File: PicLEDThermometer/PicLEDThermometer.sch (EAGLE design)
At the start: 13 parts, among them IC1 74LS595N, X1 1751248

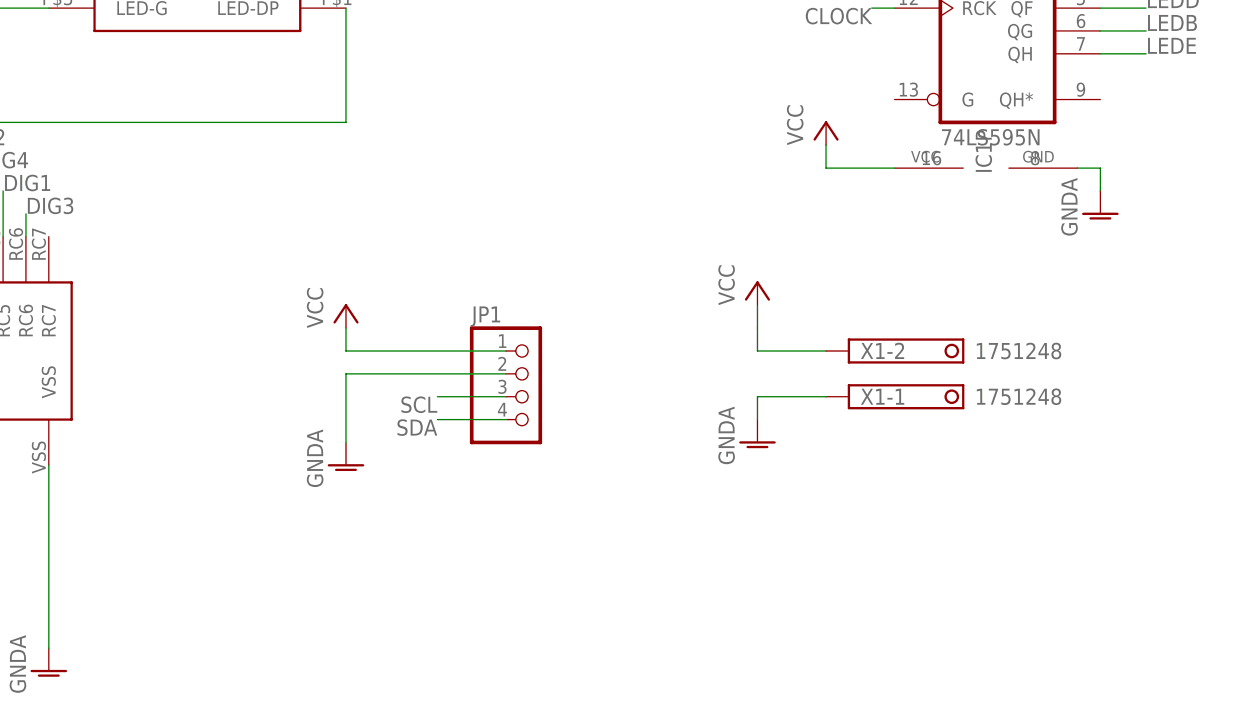
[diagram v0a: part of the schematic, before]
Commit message: Add a voltage regulator.
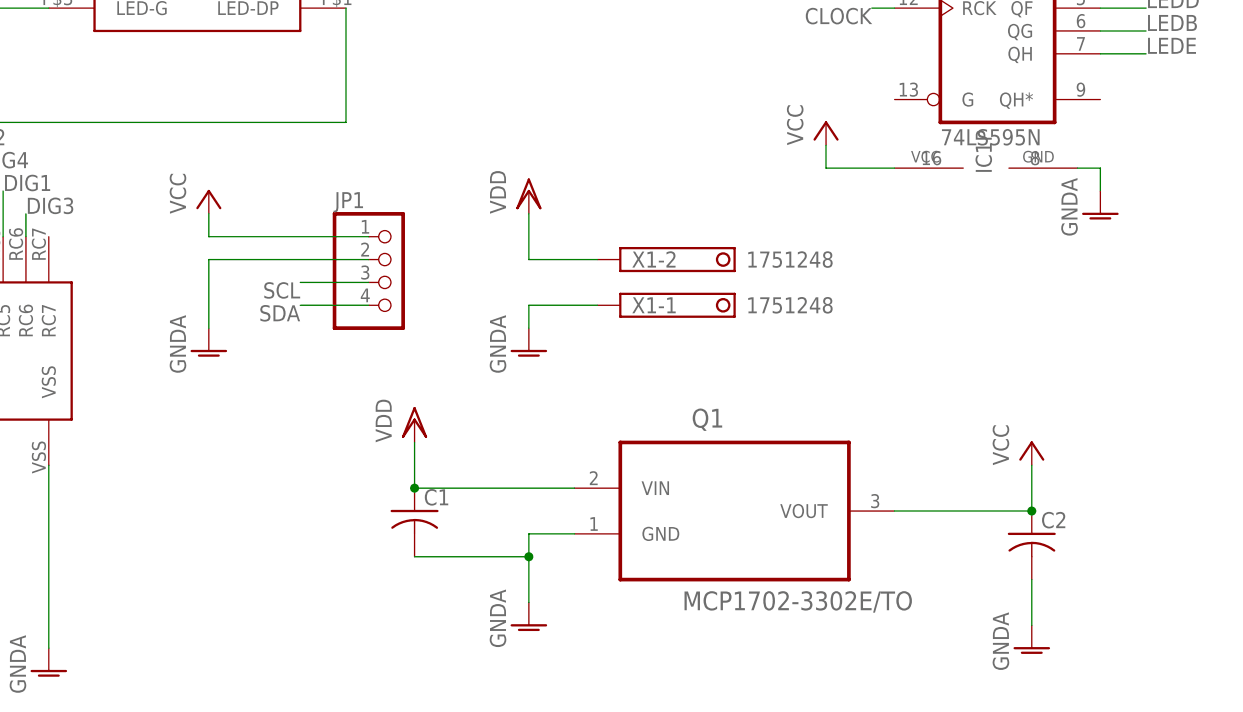
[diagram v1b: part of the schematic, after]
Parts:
- added C1, C2: (no value), rcl:C-US025-030X050
- added Q1: MCP1702-3302E/TO, Microchip_By_element14_Batch_1:MCP1702-3302E/TO
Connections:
- new net VDD: C1.1, Q1.VIN, X1-2.K
- net GNDA: now also C1.2, C2.2, Q1.GND
- net VCC: now also C2.1, Q1.VOUT; no longer X1-2.K
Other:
- moved on the sheet: JP1, X1-1, X1-2

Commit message: Change power input to padded holes.
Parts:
- removed X1: 1751248, con-phoenix-350:1751248
- added H1, H2: MOUNT-PAD-ROUND2.8, holes:MOUNT-PAD-ROUND2.8
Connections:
- net GNDA: now also H2.MOUNT; no longer X1-1.K
- net VDD: now also H1.MOUNT; no longer X1-2.K
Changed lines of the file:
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@@
 <?xml version="1.0" encoding="utf-8"?>
 <!DOCTYPE eagle SYSTEM "eagle.dtd">
-<eagle version="9.1.3">
+<eagle version="8.2.2">
 <drawing>
 <settings>
 <setting alwaysvectorfont="no"/>
-<setting keepoldvectorfont="yes"/>
 <setting verticaltext="up"/>
 </settings>
@@
 <part name="GND3" library="supply1" library_urn="urn:adsk.eagle:library:371" deviceset="GNDA" device=""/>
 <part name="P+3" library="supply1" library_urn="urn:adsk.eagle:library:371" deviceset="VCC" device=""/>
-<part name="X1" library="con-phoenix-350" library_urn="urn:adsk.eagle:library:174" deviceset="1751248" device=""/>
-<part name="GND4" library="supply1" library_urn="urn:adsk.eagle:library:371" deviceset="GNDA" device=""/>
 <part name="Q1" library="Microchip_By_element14_Batch_1" deviceset="MCP1702-3302E/TO" device=""/>
 <part name="GND5" library="supply1" library_urn="urn:adsk.eagle:library:371" deviceset="GNDA" device=""/>
 <part name="P+5" library="supply1" library_urn="urn:adsk.eagle:library:371" deviceset="VCC" device=""/>
 <part name="VDD1" library="supply1" deviceset="VDD" device=""/>
-<part name="VDD2" library="supply1" deviceset="VDD" device=""/>
-<part name="C1" library="rcl" library_urn="urn:adsk.eagle:library:334" deviceset="C-US" device="025-030X050" package3d_urn="urn:adsk.eagle:package:23631/1"/>
-<part name="C2" library="rcl" library_urn="urn:adsk.eagle:library:334" deviceset="C-US" device="025-030X050" package3d_urn="urn:adsk.eagle:package:23631/1"/>
+<part name="C1" library="rcl" library_urn="urn:adsk.eagle:library:334" deviceset="C-US" device="025-030X050"/>
+<part name="C2" library="rcl" library_urn="urn:adsk.eagle:library:334" deviceset="C-US" device="025-030X050"/>
 <part name="GND6" library="supply1" library_urn="urn:adsk.eagle:library:371" deviceset="GNDA" device=""/>
+<part name="H1" library="holes" library_urn="urn:adsk.eagle:library:237" deviceset="MOUNT-PAD-ROUND" device="2.8" value="MOUNT-PAD-ROUND2.8"/>
+<part name="H2" library="holes" library_urn="urn:adsk.eagle:library:237" deviceset="MOUNT-PAD-ROUND" device="2.8" value="MOUNT-PAD-ROUND2.8"/>
+<part name="VDD3" library="supply1" deviceset="VDD" device=""/>
+<part name="GND7" library="supply1" library_urn="urn:adsk.eagle:library:371" deviceset="GNDA" device=""/>
 </parts>
 <sheets>
@@
 <instance part="GND3" gate="1" x="170.18" y="40.64"/>
 <instance part="P+3" gate="VCC" x="139.7" y="50.8"/>
-<instance part="X1" gate="-1" x="116.84" y="30.48"/>
-<instance part="X1" gate="-2" x="116.84" y="35.56"/>
-<instance part="GND4" gate="1" x="106.68" y="25.4"/>
 <instance part="Q1" gate="A" x="129.54" y="10.16"/>
 <instance part="GND5" gate="1" x="106.68" y="-5.08"/>
 <instance part="P+5" gate="VCC" x="162.56" y="15.24"/>
 <instance part="VDD1" gate="G$1" x="93.98" y="17.78"/>
-<instance part="VDD2" gate="G$1" x="106.68" y="43.18"/>
 <instance part="C1" gate="G$1" x="93.98" y="7.62"/>
 <instance part="C2" gate="G$1" x="162.56" y="5.08"/>
 <instance part="GND6" gate="1" x="162.56" y="-7.62"/>
+<instance part="H1" gate="G$1" x="124.46" y="38.1"/>
+<instance part="H2" gate="G$1" x="124.46" y="30.48"/>
+<instance part="VDD3" gate="G$1" x="114.3" y="43.18"/>
+<instance part="GND7" gate="1" x="114.3" y="25.4"/>
 </instances>
 <busses>
@@
 <pinref part="GND3" gate="1" pin="GNDA"/>
 <wire x1="170.18" y1="45.72" x2="170.18" y2="43.18" width="0.1524" layer="91"/>
-</segment>
-<segment>
-<pinref part="GND4" gate="1" pin="GNDA"/>
-<wire x1="106.68" y1="30.48" x2="106.68" y2="27.94" width="0.1524" layer="91"/>
-<pinref part="X1" gate="-1" pin="K"/>
-<wire x1="114.3" y1="30.48" x2="106.68" y2="30.48" width="0.1524" layer="91"/>
 </segment>
 <segment>
@@
 <wire x1="162.56" y1="0" x2="162.56" y2="-5.08" width="0.1524" layer="91"/>
 </segment>
+<segment>
+<pinref part="GND7" gate="1" pin="GNDA"/>
+<wire x1="114.3" y1="30.48" x2="114.3" y2="27.94" width="0.1524" layer="91"/>
+<pinref part="H2" gate="G$1" pin="MOUNT"/>
+<wire x1="114.3" y1="30.48" x2="121.92" y2="30.48" width="0.1524" layer="91"/>
+</segment>
 </net>
 <net name="N$1" class="0">
@@
 <net name="VDD" class="0">
 <segment>
-<pinref part="X1" gate="-2" pin="K"/>
-<wire x1="114.3" y1="35.56" x2="106.68" y2="35.56" width="0.1524" layer="91"/>
-<wire x1="106.68" y1="35.56" x2="106.68" y2="40.64" width="0.1524" layer="91"/>
-<pinref part="VDD2" gate="G$1" pin="VDD"/>
-</segment>
-<segment>
 <pinref part="VDD1" gate="G$1" pin="VDD"/>
 <wire x1="93.98" y1="15.24" x2="93.98" y2="10.16" width="0.1524" layer="91"/>
@@
 <pinref part="C1" gate="G$1" pin="1"/>
 <junction x="93.98" y="10.16"/>
+</segment>
+<segment>
+<pinref part="VDD3" gate="G$1" pin="VDD"/>
+<wire x1="114.3" y1="38.1" x2="114.3" y2="40.64" width="0.1524" layer="91"/>
+<pinref part="H1" gate="G$1" pin="MOUNT"/>
+<wire x1="114.3" y1="38.1" x2="121.92" y2="38.1" width="0.1524" layer="91"/>
 </segment>
 </net>
@@
 <compatibility>
 <note version="8.2" severity="warning">
-Since Version 8.2, EAGLE supports online libraries. The ids
+Since Version 8.2, Eagle supports online libraries. The ids
 of those online libraries will not be understood (or retained)
 with this version.
 </note>
-<note version="8.3" severity="warning">
-Since Version 8.3, EAGLE supports URNs for individual library
-assets (packages, symbols, and devices). The URNs of those assets
-will not be understood (or retained) with this version.
-</note>
-<note version="8.3" severity="warning">
-Since Version 8.3, EAGLE supports the association of 3D packages
-with devices in libraries, schematics, and board files. Those 3D
-packages will not be understood (or retained) with this version.
-</note>
-<note version="8.4" severity="warning">
-Since Version 8.4, EAGLE supports properties for SPICE simulation.
-Probes in schematics and SPICE mapping objects found in parts and library devices
-will not be understood with this version. Update EAGLE to the latest version
-for full support of SPICE simulation.
-</note>
 </compatibility>
